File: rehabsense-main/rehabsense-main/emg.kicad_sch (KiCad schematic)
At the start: 21 parts, among them U7 TL074

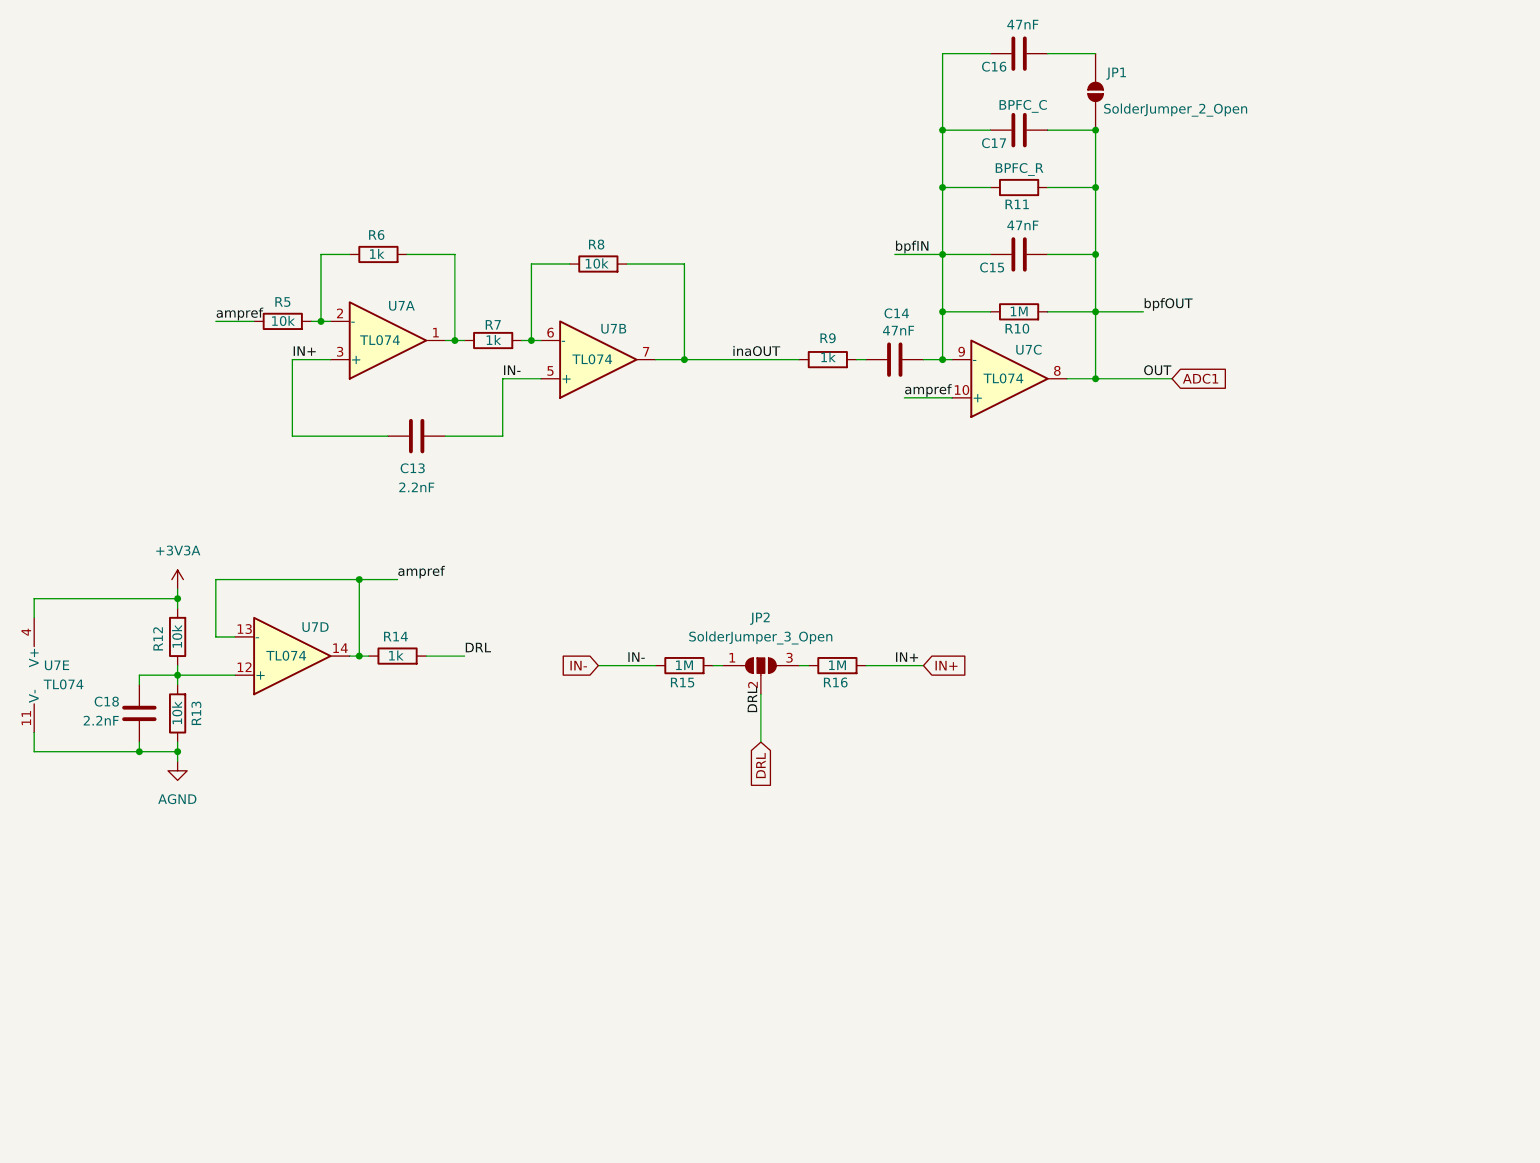
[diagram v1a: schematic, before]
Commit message: Adding adcs
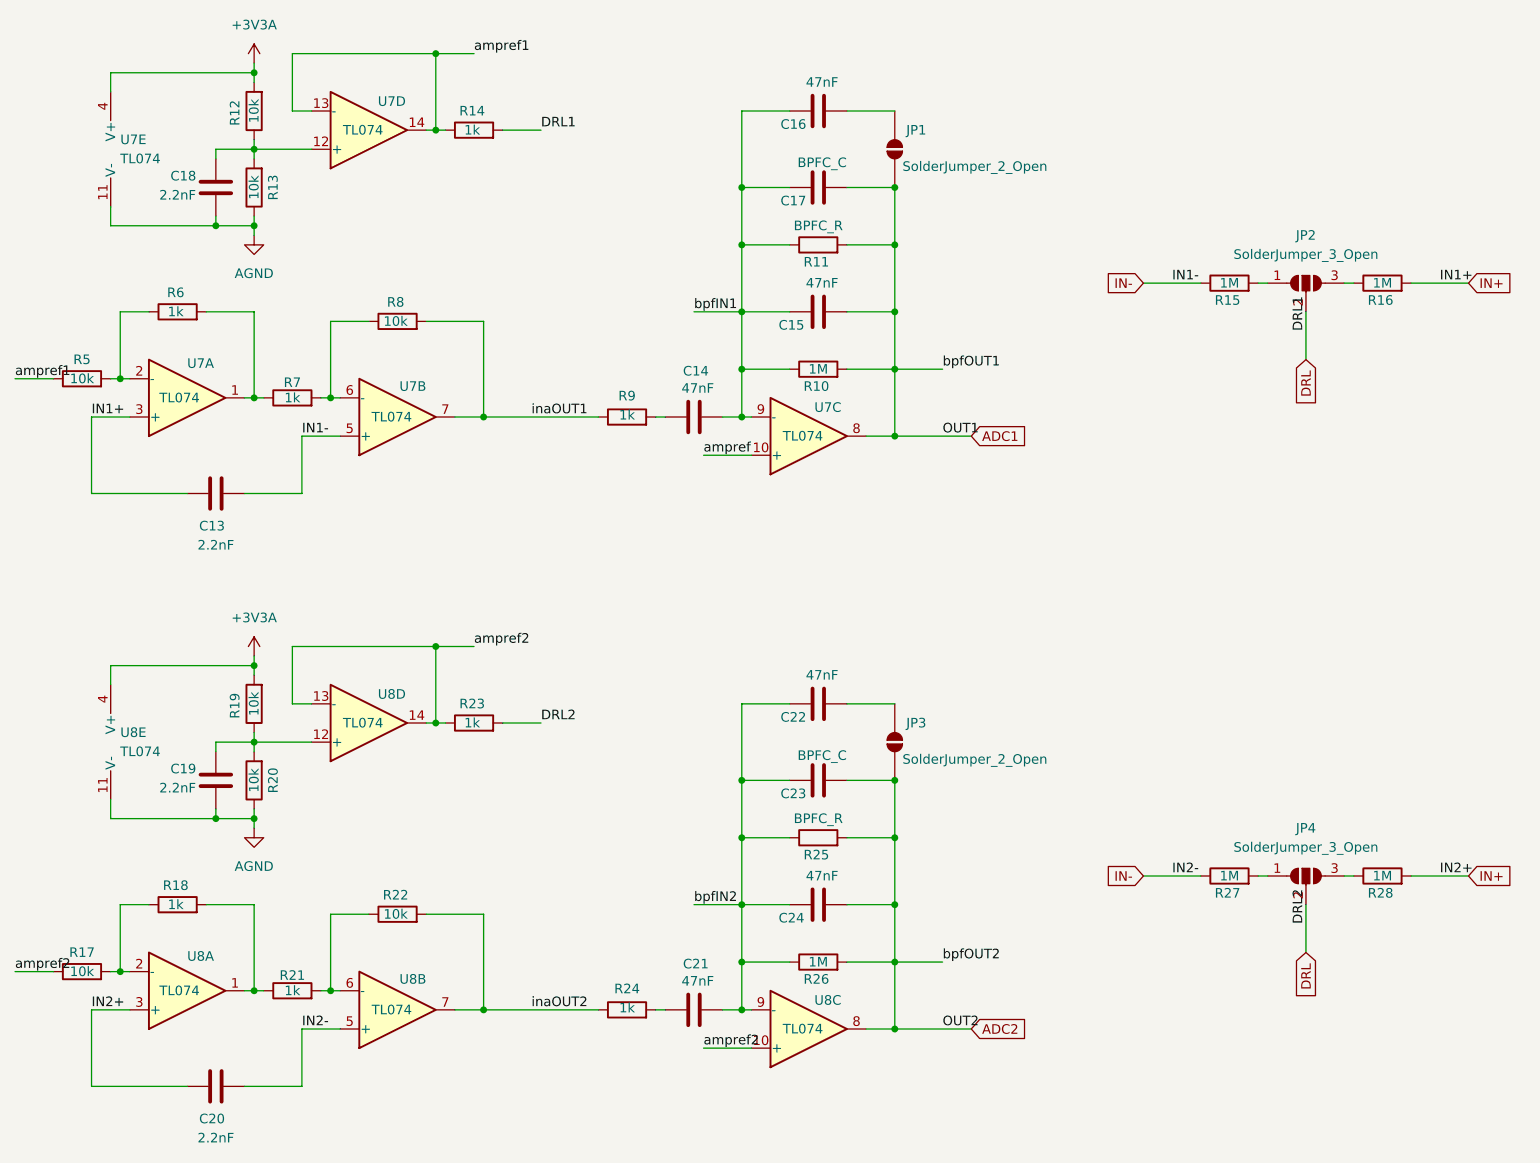
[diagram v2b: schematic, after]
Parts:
- added C19, C20: 2.2nF, symbol Device:C
- added C21, C22, C24: 47nF, symbol Device:C
- added C23: BPFC_C, symbol Device:C
- added JP3: SolderJumper_2_Open, symbol Jumper:SolderJumper_2_Open
- added JP4: SolderJumper_3_Open, symbol Jumper:SolderJumper_3_Open
- added R17, R19, R20, R22: 10k, symbol Device:R
- added R18, R21, R23, R24: 1k, symbol Device:R
- added R25: BPFC_R, symbol Device:R
- added R26, R27, R28: 1M, symbol Device:R
- added U8: TL074, symbol Amplifier_Operational:TL074
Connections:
- net +3V3A: now also R19.2, U8.4 (V+)
- net AGND: now also C19.1, R20.1, U8.11 (V-)
- net DRL: now also JP4.2 (C), R23.2
- net IN+: now also C20.1, R28.2, U8.3 (+)
- net IN-: now also C20.2, R27.1, U8.5 (+)
- net ampref: no longer R14.1, R5.1, U7.13 (-), U7.14
- net bpfIN renamed bpfIN1
- net inaOUT renamed inaOUT1
- new net: R18.2, R21.1, U8.1
- new net: R17.2, R18.1, U8.2 (-)
- new net: C22.2, JP3.2 (B)
- new net: R21.2, R22.1, U8.6 (-)
- new net: JP4.3 (B), R28.1
- new net: C21.1, R24.2
- new net: C19.2, R19.1, R20.2, U8.12 (+)
- new net: JP4.1 (A), R27.2
- new net ADC2: C23.2, C24.2, JP3.1 (A), R25.2, R26.2, U8.8
- new net ampref1: R14.1, R5.1, U7.13 (-), U7.14
- new net ampref2: R17.1, R23.1, U8.10 (+), U8.13 (-), U8.14
- new net bpfIN2: C21.2, C22.1, C23.1, C24.1, R25.1, R26.1, U8.9 (-)
- new net inaOUT2: R22.2, R24.1, U8.7
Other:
- moved on the sheet: C13, C14, C15, C16, C17, C18, JP1, JP2, R10, R11, R12, R13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
